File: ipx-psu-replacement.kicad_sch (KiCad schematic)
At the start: 16 parts, among them J1 L, J10 -12V, J11 GND, J2 AC IN, J3 GND, J4 Floppy, J5 AC OUT, J6 N, J7 +12V, J8 +5V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

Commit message: add power good sensing
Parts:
- added C1, C2: 100n, Capacitor_SMD:C_0201_0603Metric_Pad0.64x0.40mm_HandSolder, symbol Device:C_Small
- added J12: Fan, Connector_PinHeader_2.54mm:PinHeader_1x02_P2.54mm_Vertical, symbol Connector:Conn_01x02_Pin
- added J13: SENS, Connector_Wire:SolderWire-1.5sqmm_1x01_D1.7mm_OD3mm, symbol Connector:Conn_01x01_Pin
- added U1: 74HCT27, Package_SO:SO-14_3.9x8.65mm_P1.27mm, symbol 74xx:74LS27
- added U2: MAX8215, Package_SO:SO-14_3.9x8.65mm_P1.27mm, symbol Power_Supervisor:MAX8215
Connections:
- net +12V: now also J12.2 (Pin_2), U2.5 (+12V)
- net +5V: now also C1.1, C2.1, U1.14 (VCC), U2.14 (VDD), U2.3 (+5V)
- net -12V: now also U2.6 (-12V)
- net GND: now also C1.2, C2.2, J12.1 (Pin_1), U1.1, U1.10, U1.11, U1.13, U1.2, U1.7 (GND), U1.9, U2.2 (GND), U2.8 (PGND)
- new net: J13.1 (Pin_1), U1.6
- new net: U1.5, U2.10 (OUT4)
- new net: U1.4, U2.11 (OUT3)
- new net: U1.3, U2.13 (OUT1)
- no-connect marks 2 -> 9
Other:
- moved on the sheet: D1, F1, J2, J5, K1, PS1, PS2

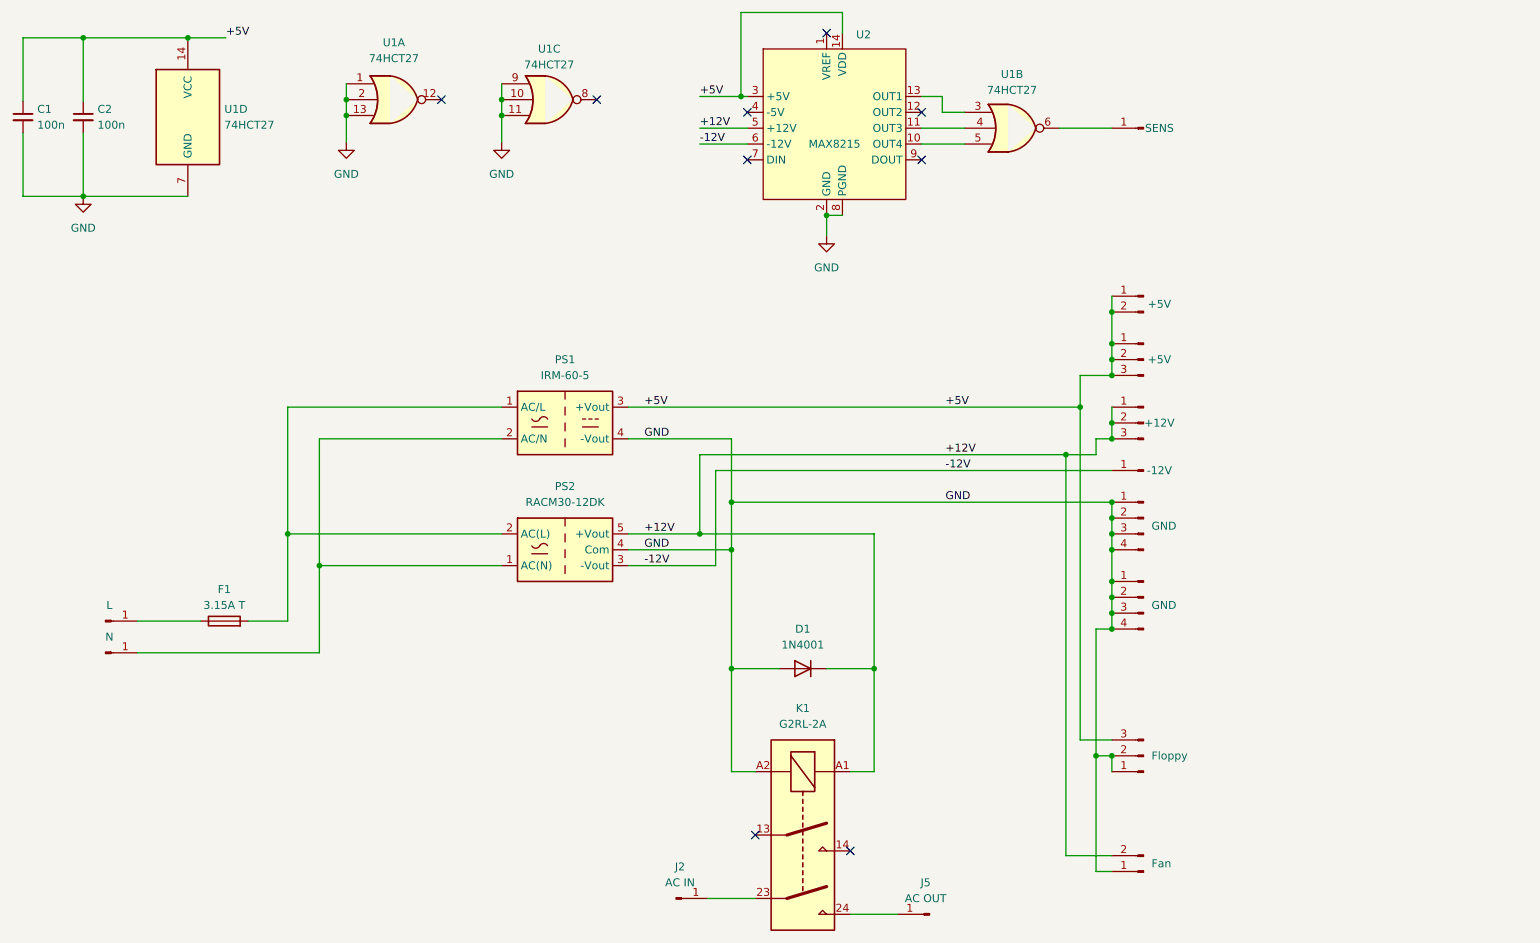
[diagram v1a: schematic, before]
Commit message: supervisor circuitry fixed & improved
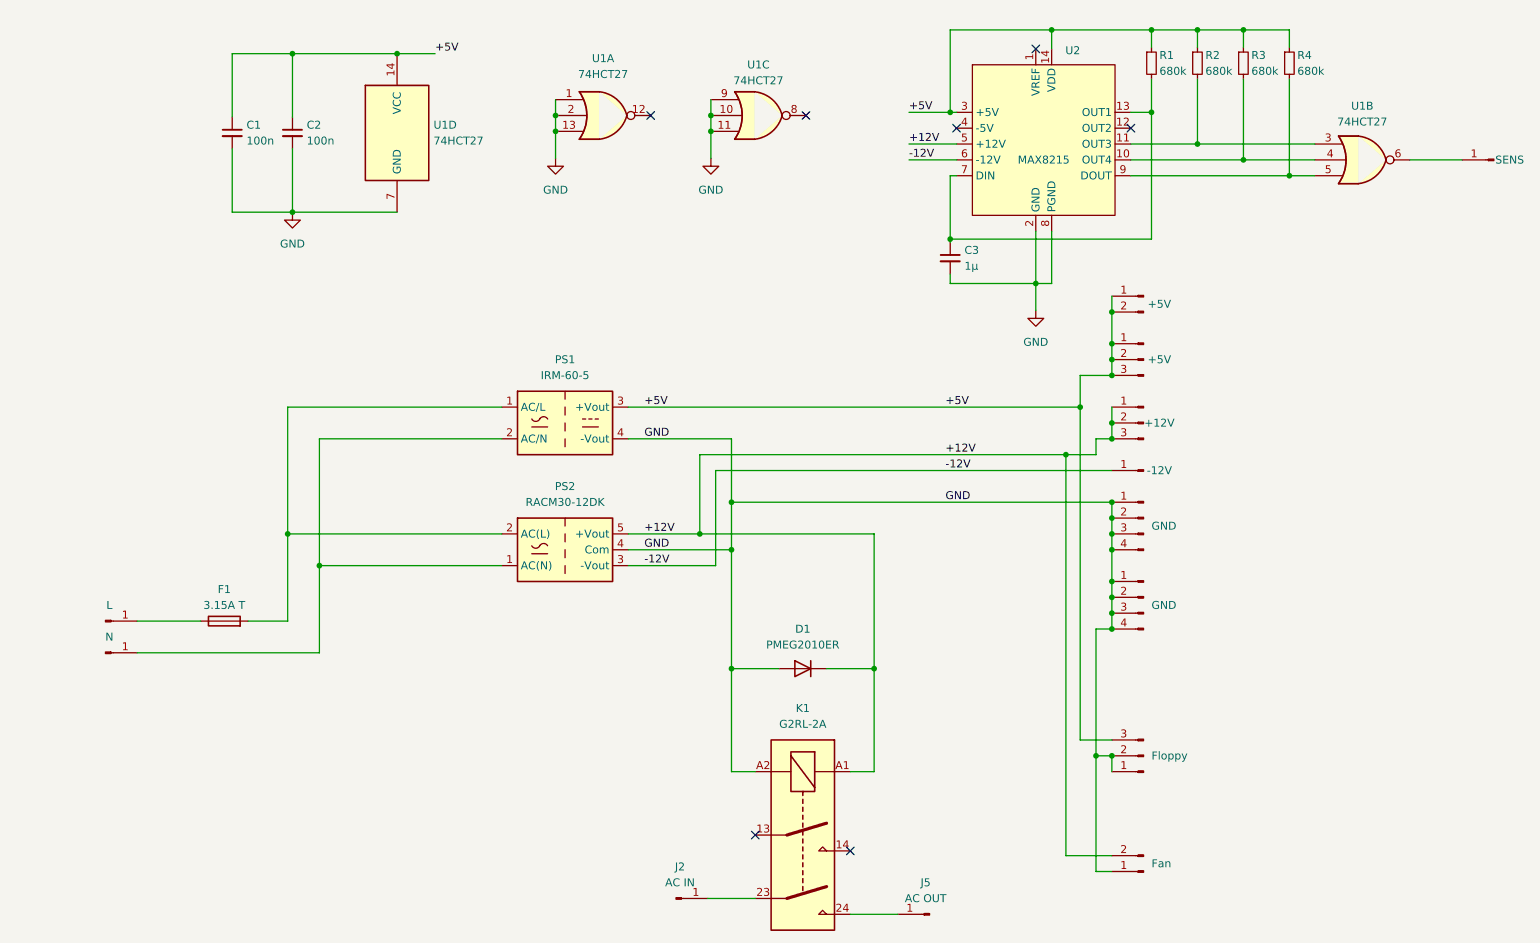
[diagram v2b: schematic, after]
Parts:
- added C3: 1µ, Capacitor_SMD:C_0603_1608Metric_Pad1.08x0.95mm_HandSolder, symbol Device:C_Small
- added R1, R2, R3, R4: 680k, Resistor_SMD:R_0603_1608Metric_Pad0.98x0.95mm_HandSolder, symbol Device:R_Small
- C1, C2: footprint Capacitor_SMD:C_0201_0603Metric_Pad0.64x0.40mm_HandSolder -> Capacitor_SMD:C_0603_1608Metric_Pad1.08x0.95mm_HandSolder
- D1: value 1N4001 -> PMEG2010ER; footprint Diode_THT:D_DO-41_SOD81_P7.62mm_Horizontal -> Diode_SMD:D_SOD-123
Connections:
- net +5V: now also R1.1, R2.1, R3.1, R4.1
- net GND: now also C3.2
- net at U1.5: now also U2.9 (DOUT), R4.2; no longer U2.10 (OUT4)
- net at U1.4: now also U2.10 (OUT4), R3.2; no longer U2.11 (OUT3)
- net at U2.13 (OUT1): now also U2.7 (DIN), C3.1, R1.2; no longer U1.3
- new net: R2.2, U1.3, U2.11 (OUT3)
- no-connect marks 9 -> 7
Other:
- moved on the sheet: C1, C2, U1A, U1B, U1C, U1D, U2

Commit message: more adjustments
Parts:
- added J14, J15: GND, Connector_Wire:SolderWire-2sqmm_1x01_D2mm_OD3.9mm, symbol Connector:Conn_01x01_Pin
- F1: footprint Fuse:Fuseholder_Clip-5x20mm_Bel_FC-203-22_Lateral_P17.80x5.00mm_D1.17mm_Horizontal -> Fuse:Fuseholder_Clip-5x20mm_Littelfuse_111_Inline_P20.00x5.00mm_D1.05mm_Horizontal
- K1: value G2RL-2A -> DH2U TV3
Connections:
- net GND: now also J14.1 (Pin_1), J15.1 (Pin_1)
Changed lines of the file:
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@@
   (junction (at 194.31 87.63) (diameter 0) (color 0 0 0 0)
+  )
+  (junction (at 245.872 70.104) (diameter 0) (color 0 0 0 0)
   )
   (junction (at 194.31 105.41) (diameter 0) (color 0 0 0 0)
@@
     (stroke (width 0) (type default))
   )
+  (wire (pts (xy 245.872 70.104) (xy 245.872 76.2))
+    (stroke (width 0) (type default))
+  )
   (wire (pts (xy 169.418 45.466) (xy 168.402 45.466))
     (stroke (width 0) (type default))
@@
     (stroke (width 0) (type default))
   )
+  (wire (pts (xy 239.522 70.104) (xy 245.872 70.104))
+    (stroke (width 0) (type default))
+  )
   (wire (pts (xy 194.31 135.89) (xy 189.23 135.89))
     (stroke (width 0) (type default))
@@
   )
   (label "+5V" (at 167.64 82.55 0) (fields_autoplaced)
+    (effects (font (size 1.27 1.27)) (justify left bottom))
+  )
+  (label "GND" (at 239.522 70.104 0) (fields_autoplaced)
     (effects (font (size 1.27 1.27)) (justify left bottom))
   )
@@
     )
   )
+  (symbol (lib_id "Connector:Conn_01x01_Pin") (at 250.952 76.2 180) (unit 1)
+    (in_bom yes) (on_board yes) (dnp no)
+    (property "Reference" "J15" (at 250.317 70.866 0)
+      (effects (font (size 1.27 1.27)) hide)
+    )
+    (property "Value" "GND" (at 250.317 73.406 0)
+      (effects (font (size 1.27 1.27)))
+    )
+    (property "Footprint" "Connector_Wire:SolderWire-2sqmm_1x01_D2mm_OD3.9mm" (at 250.952 76.2 0)
+      (effects (font (size 1.27 1.27)) hide)
+    )
+    (property "Datasheet" "~" (at 250.952 76.2 0)
+      (effects (font (size 1.27 1.27)) hide)
+    )
+    (pin "1")
+    (instances
+      (project "ipx-psu-replacement"
+        (path "/80e599cc-36ff-4f54-a2a4-590742b133b5"
+          (reference "J15") (unit 1)
+        )
+      )
+    )
+  )
   (symbol (lib_id "Device:C_Small") (at 168.402 58.674 0) (unit 1)
     (in_bom yes) (on_board yes) (dnp no)
@@
     (in_bom yes) (on_board yes) (dnp no) (fields_autoplaced)
     (property "Reference" "K1" (at 144.78 130.81 90)
-      (effects (font (size 1.27 1.27)))
-    )
-    (property "Value" "G2RL-2A" (at 144.78 133.35 90)
+      (effects (font (size 1.27 1.27)) hide)
+    )
+    (property "Value" "DH2U TV3" (at 144.78 133.35 90)
       (effects (font (size 1.27 1.27)))
     )
@@
         (path "/80e599cc-36ff-4f54-a2a4-590742b133b5"
           (reference "J8") (unit 1)
+        )
+      )
+    )
+  )
+  (symbol (lib_id "Connector:Conn_01x01_Pin") (at 250.952 70.104 180) (unit 1)
+    (in_bom yes) (on_board yes) (dnp no) (fields_autoplaced)
+    (property "Reference" "J14" (at 250.317 64.77 0)
+      (effects (font (size 1.27 1.27)) hide)
+    )
+    (property "Value" "GND" (at 250.317 67.31 0)
+      (effects (font (size 1.27 1.27)))
+    )
+    (property "Footprint" "Connector_Wire:SolderWire-2sqmm_1x01_D2mm_OD3.9mm" (at 250.952 70.104 0)
+      (effects (font (size 1.27 1.27)) hide)
+    )
+    (property "Datasheet" "~" (at 250.952 70.104 0)
+      (effects (font (size 1.27 1.27)) hide)
+    )
+    (pin "1")
+    (instances
+      (project "ipx-psu-replacement"
+        (path "/80e599cc-36ff-4f54-a2a4-590742b133b5"
+          (reference "J14") (unit 1)
         )
       )
@@
       (effects (font (size 1.27 1.27)))
     )
-    (property "Footprint" "Fuse:Fuseholder_Clip-5x20mm_Bel_FC-203-22_Lateral_P17.80x5.00mm_D1.17mm_Horizontal" (at 52.07 118.618 90)
-      (effects (font (size 1.27 1.27)) hide)
-    )
+    (property "Footprint" "Fuse:Fuseholder_Clip-5x20mm_Littelfuse_111_Inline_P20.00x5.00mm_D1.05mm_Horizontal" (at 52.07 118.618 90)
+      (effects (font (size 1.27 1.27)) hide)
+    )

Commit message: v1 - sent to production
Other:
- moved on the sheet: C1, C2, C3, R1, R2, R3, R4, U1A, U1B, U1C, U1D, U2
